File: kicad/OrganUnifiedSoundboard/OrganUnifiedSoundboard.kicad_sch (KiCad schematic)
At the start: 0 parts

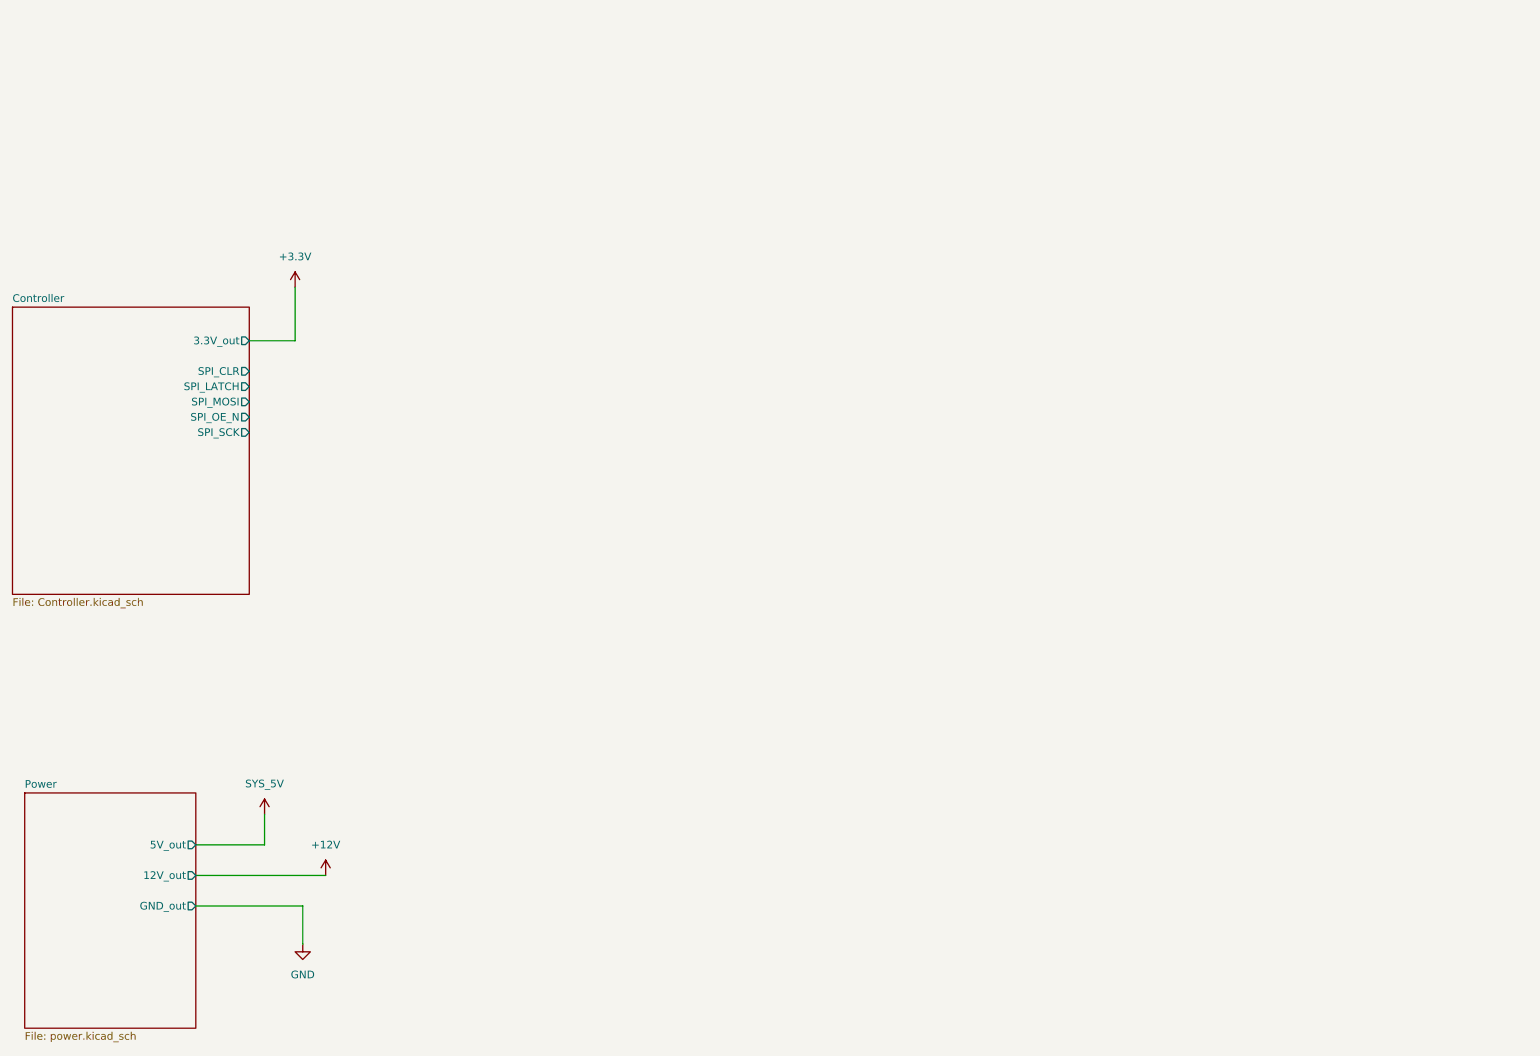
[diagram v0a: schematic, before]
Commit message: Adding some custom components that some of the kicad things depend on
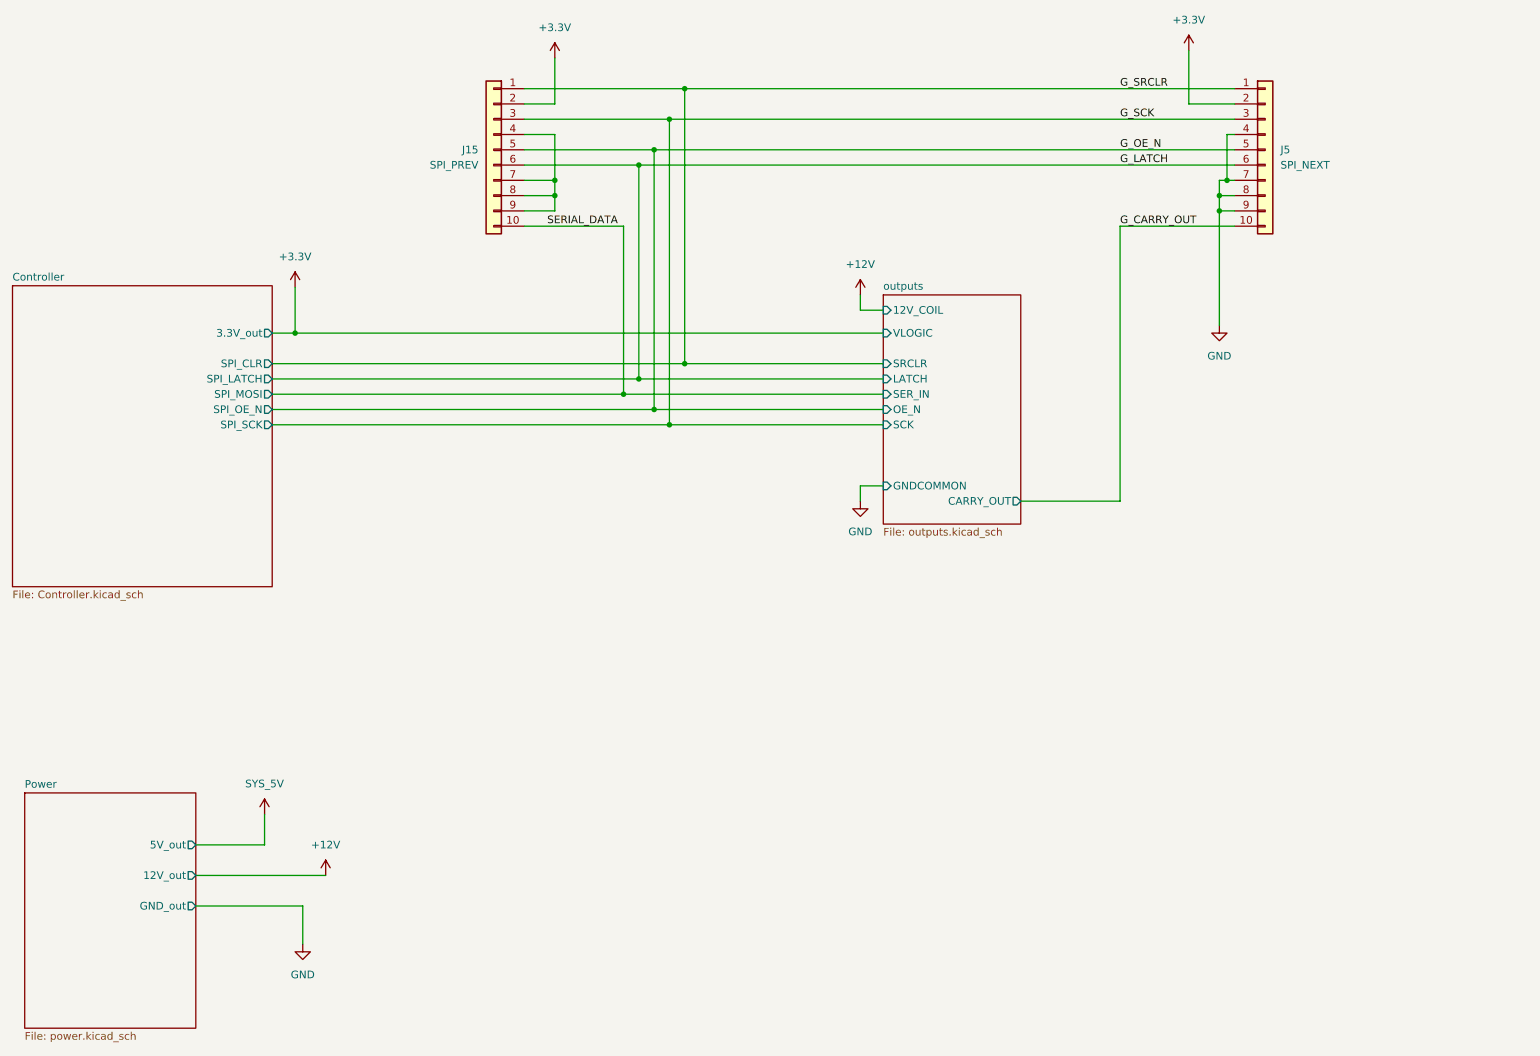
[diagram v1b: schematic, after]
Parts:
- added J15: SPI_PREV, Connector_IDC:IDC-Header_2x05_P2.54mm_Vertical, symbol Connector_Generic:Conn_01x10
- added J5: SPI_NEXT, Connector_IDC:IDC-Header_2x05_P2.54mm_Vertical, symbol Connector_Generic:Conn_01x10
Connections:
- net +3.3V: now also J15.2 (Pin_2), J5.2 (Pin_2)
- net GND: now also J5.4 (Pin_4), J5.7 (Pin_7), J5.8 (Pin_8), J5.9 (Pin_9)
- new net: J15.4 (Pin_4), J15.7 (Pin_7), J15.8 (Pin_8), J15.9 (Pin_9)
- new net G_CARRY_OUT: J5.10 (Pin_10)
- new net G_LATCH: J15.6 (Pin_6), J5.6 (Pin_6)
- new net G_OE_N: J15.5 (Pin_5), J5.5 (Pin_5)
- new net G_SCK: J15.3 (Pin_3), J5.3 (Pin_3)
- new net G_SRCLR: J15.1 (Pin_1), J5.1 (Pin_1)
- new net SERIAL_DATA: J15.10 (Pin_10)
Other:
- added sheet outputs (outputs.kicad_sch)

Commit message: Finalized unified soundboard driver for production, adding some models
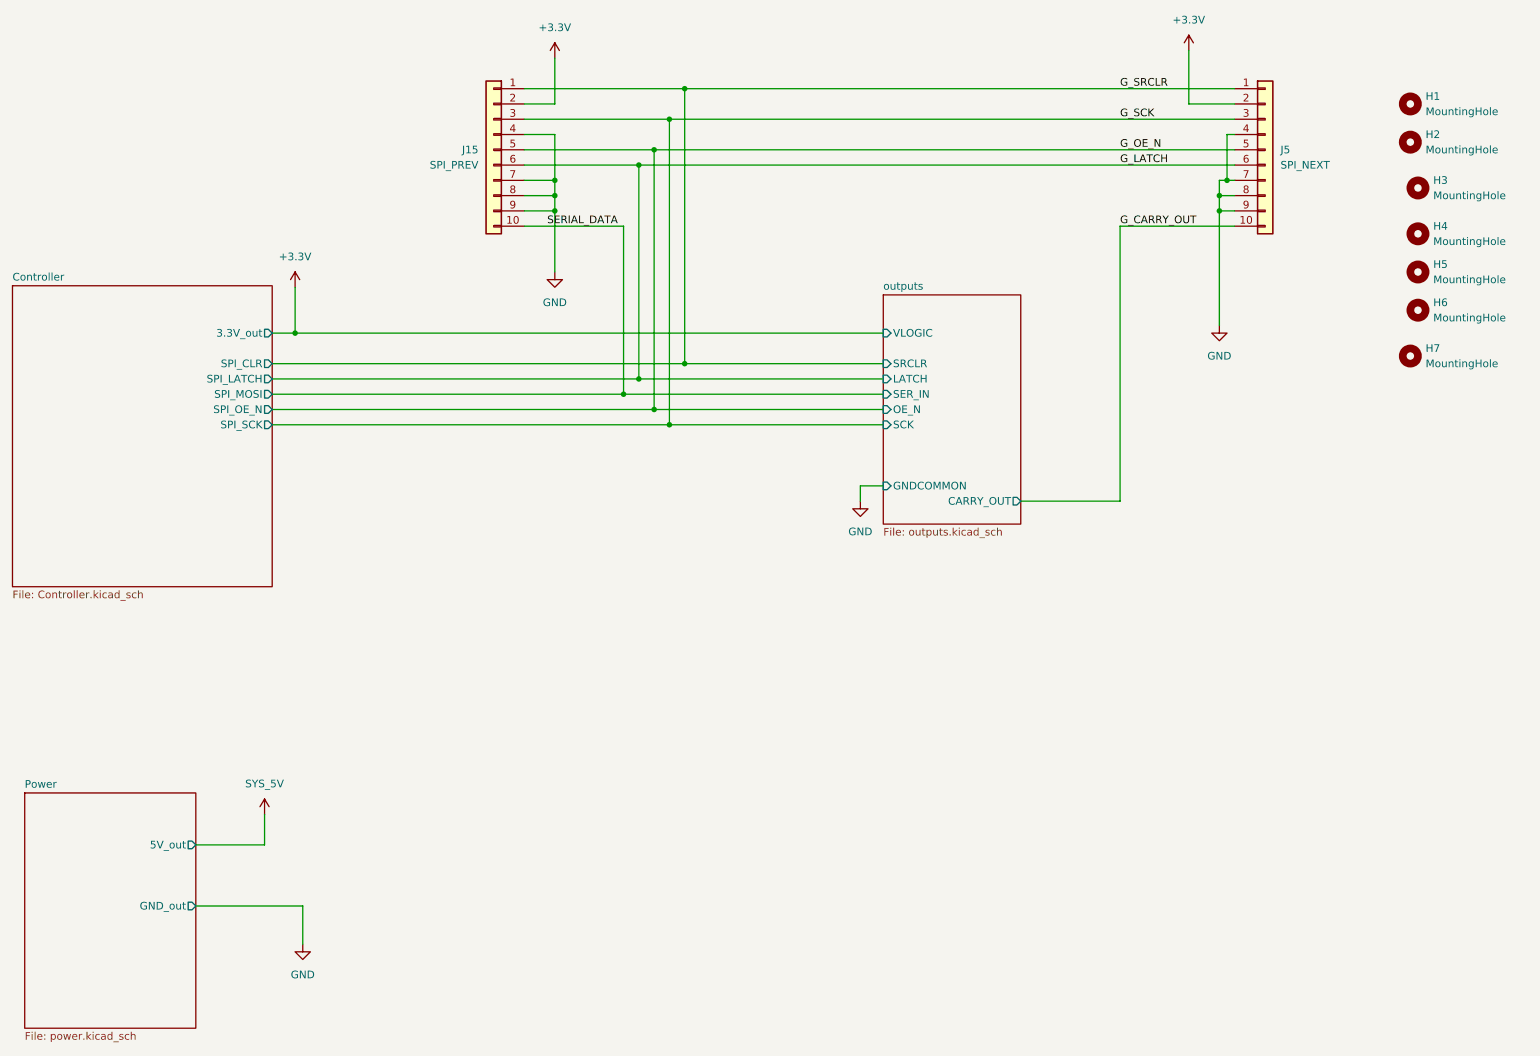
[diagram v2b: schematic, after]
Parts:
- added H1, H2, H3, H4, H5, H6, H7: MountingHole, MountingHole:MountingHole_3.2mm_M3, symbol Mechanical:MountingHole
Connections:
- net GND: now also J15.4 (Pin_4), J15.7 (Pin_7), J15.8 (Pin_8), J15.9 (Pin_9)
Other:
- sheet Power ports: added none; removed 12V_out
- sheet outputs ports: added none; removed 12V_COIL
